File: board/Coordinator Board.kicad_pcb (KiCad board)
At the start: 4 copper layers, 45.5 x 39.6 mm, 30 parts, among them J1 Conn_01x04, J2 Conn_01x04, J3 Conn_01x04, P4 SERIAL, SW1 Switch_SPDT_x2, SW2 Switch_DPST, U0 10118194, U1 LM3671, U2 CD74HC4050, U3 ESP-12E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

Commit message: Finished and ordered v3.0 of the board!!
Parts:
- U2: moved to B.Cu
- moved J3 2.93 mm to (126.1, 132.4)
- moved C6 2.93 mm to (128.6, 136.2)
- moved D1 2.19 mm to (131.8, 121.8), turned to 180 degrees
- moved SW2 2.10 mm to (131.9, 118.7)
- moved U5 2.05 mm to (131.9, 110.0)
- moved U2 2.03 mm to (120.3, 135.9)
- moved R8 1.82 mm to (131.9, 124.2), turned to 180 degrees
- moved C4 1.45 mm to (110.8, 133.8)
- moved J2 1.35 mm to (114.7, 131.2)
- moved L1 1.05 mm to (107.0, 127.7)
- moved P4 0.68 mm to (130.4, 128.3)
- moved C5 0.25 mm to (101.8, 135.9)
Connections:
- U3 pad 13: Net-(RP1-Pad4) -> Net-(RP1-Pad3)
- U3 pad 14: Net-(RP1-Pad3) -> Net-(RP1-Pad4)
- U5 pad 1: Net-(R7-Pad2) -> Net-(RP1-Pad2)
- U5 pad 2: Net-(RP1-Pad2) -> Net-(RP1-Pad1)
- U5 pad 3: Net-(RP1-Pad1) -> Net-(R7-Pad2)
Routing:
- net Net-(D1-Pad2): track 41.6 -> 32.4 mm
- net Net-(R2-Pad1): track 39.6 -> 45.1 mm, vias 2 -> 3
- net Net-(U2-Pad3): track 13.9 -> 19.0 mm, vias 0 -> 3
- net Net-(J1-Pad2): track 23.8 -> 19.8 mm, vias 1 -> 0
- net Net-(U2-Pad11): track 17.0 -> 20.8 mm, vias 0 -> 3
- net GND: track 63.9 -> 60.4 mm, vias 7 -> 8
- net Net-(J3-Pad2): track 6.38 -> 3.21 mm
- net Net-(J1-Pad3): track 16.3 -> 13.6 mm
- net Net-(RP1-Pad2): track 44.7 -> 42.1 mm
- net Net-(R7-Pad2): track 45.5 -> 43.0 mm
- net Net-(J3-Pad3): track 12.0 -> 9.95 mm, vias 1 -> 0
- net Net-(RP1-Pad4): track 37.5 -> 36.0 mm
- net +5V: track 21.9 -> 23.2 mm, vias 4 -> 3
- net Net-(RP1-Pad1): track 48.6 -> 49.6 mm, vias 3 -> 2
- net Net-(J2-Pad2): track 14.7 -> 13.7 mm, vias 2 -> 1
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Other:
- board size 45.5 x 39.6 mm -> 42.5 x 38.5 mm
- board text added: "Raver Lights Hub v3.0 Copyright Bryan Hughes 2018"
- board text removed: "Raver Lights Coordinator v3.0 Copyright Bryan Hughes 2018"
- board text removed: "STS"

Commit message: Updated through first build
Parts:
- added C3: 0.1uF, Capacitors_SMD:C_0805_HandSoldering, F.Cu at (87.7, 125.6)
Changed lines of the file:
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@@
 (kicad_pcb (version 4) (host pcbnew 4.0.7)
   (general
-    (links 93)
-    (no_connects 0)
+    (links 95)
+    (no_connects 2)
     (area 93.869999 103.109999 136.515001 141.691001)
     (thickness 1.6)
@@
     (tracks 346)
     (zones 0)
-    (modules 30)
+    (modules 31)
     (nets 33)
   )
@@
   )
   (setup
-    (last_trace_width 0.3048)
+    (last_trace_width 0.1524)
     (user_trace_width 0.1524)
     (user_trace_width 0.3048)
@@
       (net 4 GND))
   )
+  (module Capacitors_SMD:C_0805_HandSoldering (layer F.Cu)
+    (at 87.697 125.639)
+    (descr "Capacitor SMD 0805, hand soldering")
+    (tags "capacitor 0805")
+    (attr smd)
+    (fp_text reference C3 (at 0 -1.75) (layer F.SilkS)
+      (effects (font (size 1 1) (thickness 0.15)))
+    )
+    (fp_text value 0.1uF (at 0 1.75) (layer F.Fab)
+      (effects (font (size 1 1) (thickness 0.15)))
+    )
+    (fp_text user %R (at 0 -1.75) (layer F.Fab)
+      (effects (font (size 1 1) (thickness 0.15)))
+    )
+    (fp_line (start -1 0.62) (end -1 -0.62) (layer F.Fab) (width 0.1))
+    (fp_line (start 1 0.62) (end -1 0.62) (layer F.Fab) (width 0.1))
+    (fp_line (start 1 -0.62) (end 1 0.62) (layer F.Fab) (width 0.1))
+    (fp_line (start -1 -0.62) (end 1 -0.62) (layer F.Fab) (width 0.1))
+    (fp_line (start 0.5 -0.85) (end -0.5 -0.85) (layer F.SilkS) (width 0.12))
+    (fp_line (start -0.5 0.85) (end 0.5 0.85) (layer F.SilkS) (width 0.12))
+    (fp_line (start -2.25 -0.88) (end 2.25 -0.88) (layer F.CrtYd) (width 0.05))
+    (fp_line (start -2.25 -0.88) (end -2.25 0.87) (layer F.CrtYd) (width 0.05))
+    (fp_line (start 2.25 0.87) (end 2.25 -0.88) (layer F.CrtYd) (width 0.05))
+    (fp_line (start 2.25 0.87) (end -2.25 0.87) (layer F.CrtYd) (width 0.05))
+    (pad 1 smd rect (at -1.25 0) (size 1.5 1.25) (layers F.Cu F.Paste F.Mask)
+      (net 5 +3V3))
+    (pad 2 smd rect (at 1.25 0) (size 1.5 1.25) (layers F.Cu F.Paste F.Mask)
+      (net 4 GND))
+    (model Capacitors_SMD.3dshapes/C_0805.wrl
+      (at (xyz 0 0 0))
+      (scale (xyz 1 1 1))
+      (rotate (xyz 0 0 0))
+    )
+  )
   (gr_text FUSE (at 97.73 117.13 90) (layer F.SilkS)

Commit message: Initial 3.1 board redesign
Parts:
- removed C3: 0.1uF, Capacitors_SMD:C_0805_HandSoldering
- removed C4, C5, C6: 10uF, Resistors_SMD:R_0805_HandSoldering
- removed D1: LED, LEDs:LED_1206_HandSoldering
- removed R1, R4, R7: 10k, Resistors_SMD:R_0805_HandSoldering
- removed R8: 0, Resistors_SMD:R_0805_HandSoldering
- removed U2: CD74HC4050, Housings_SOIC:SOIC-16W_5.3x10.2mm_Pitch1.27mm
- added J4: Conn_01x04, Pin_Headers:Pin_Header_Angled_1x04_Pitch2.54mm, F.Cu at (124.7, 131.2)
- added RV1: POT, nebrius-discrete:Model-35-Pot, F.Cu at (132.1, 119.4)
- U6: value SN74LVC1T45 -> SN74LVC1T45 - MOSI
- U7: value SN74LVC1T45 -> SN74LVC1T45 - SCLK
- moved SW2 6.24 mm to (132.4, 124.9)
- moved J3 1.42 mm to (127.4, 132.1)
- moved J1 1.40 mm to (102.9, 139.7)
- moved J2 1.40 mm to (113.4, 131.2)
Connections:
- J2 pad 2: Net-(J2-Pad2) -> Net-(J1-Pad2)
- J2 pad 3: Net-(J2-Pad3) -> Net-(J1-Pad3)
- J3 pad 2: Net-(J3-Pad2) -> Net-(J1-Pad2)
- J3 pad 3: Net-(J3-Pad3) -> Net-(J1-Pad3)
- RP1 pad 1: Net-(RP1-Pad1) -> GND
- RP1 pad 2: Net-(RP1-Pad2) -> GND
- RP1 pad 3: Net-(RP1-Pad3) -> GND
- RP1 pad 4: Net-(RP1-Pad4) -> +3V3
- RP1 pad 5: +3V3 -> Net-(RP1-Pad5)
- RP1 pad 6: +3V3 -> Net-(RP1-Pad6)
- RP1 pad 7: +3V3 -> Net-(RP1-Pad7)
- RP1 pad 8: +3V3 -> Net-(RP1-Pad8)
- U3 pad 10: Net-(R4-Pad1) -> Net-(RP1-Pad8)
- U3 pad 11: Net-(R1-Pad2) -> Net-(RP1-Pad5)
- U3 pad 13: Net-(RP1-Pad3) -> Net-(RP1-Pad7)
- U3 pad 14: Net-(RP1-Pad4) -> Net-(RP1-Pad6)
- U3 pad 19: Net-(R7-Pad2) -> (no net)
- U3 pad 2: (no net) -> Net-(RV1-Pad2)
- U3 pad 20: Net-(D1-Pad2) -> (no net)
- U3 pad 21: Net-(U3-Pad21) -> (no net)
- U3 pad 22: Net-(U3-Pad22) -> (no net)
- U3 pad 6: Net-(RP1-Pad2) -> Net-(U3-Pad6)
- U3 pad 7: Net-(RP1-Pad1) -> Net-(U3-Pad7)
- U4 pad 3: Net-(U3-Pad4) -> Net-(U3-Pad6)
- U4 pad 4: Net-(U3-Pad5) -> Net-(U3-Pad4)
- U5 pad 1: Net-(RP1-Pad2) -> (no net)
- U5 pad 2: Net-(RP1-Pad1) -> Net-(RP1-Pad8)
- U5 pad 3: Net-(R7-Pad2) -> Net-(RP1-Pad6)
- U5 pad 4: Net-(RP1-Pad4) -> Net-(RP1-Pad7)
- U5 pad 5: GND -> +3V3
- U5 pad 6: Net-(RP1-Pad3) -> (no net)
- U6 pad 3: Net-(U2-Pad11) -> Net-(J1-Pad3)
- U6 pad 4: Net-(U3-Pad21) -> Net-(U3-Pad7)
- U7 pad 3: Net-(U2-Pad3) -> Net-(J1-Pad2)
- U7 pad 4: Net-(U3-Pad22) -> Net-(U3-Pad5)
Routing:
- net GND: track 60.4 -> 0.00 mm, vias 8 -> 0
- net Net-(RP1-Pad1): track 49.6 -> 0.00 mm, vias 2 -> 0
- net Net-(U3-Pad22): track 45.5 -> 0.00 mm, vias 1 -> 0
- net Net-(R2-Pad1): track 45.1 -> 0.00 mm, vias 3 -> 0
- net Net-(R7-Pad2): track 43.0 -> 0.00 mm, vias 2 -> 0
- net Net-(RP1-Pad3): track 42.4 -> 0.00 mm, vias 2 -> 0
- net Net-(RP1-Pad2): track 42.1 -> 0.00 mm, vias 2 -> 0
- net Net-(U3-Pad21): track 41.4 -> 0.00 mm, vias 1 -> 0
- net Net-(P4-Pad2): track 36.1 -> 0.00 mm, vias 1 -> 0
- net Net-(RP1-Pad4): track 36.0 -> 0.00 mm, vias 2 -> 0
- net Net-(P4-Pad1): track 34.2 -> 0.00 mm, vias 1 -> 0
- net Net-(D1-Pad2): track 32.4 -> 0.00 mm, vias 1 -> 0
- net +3V3: track 29.7 -> 0.00 mm, vias 5 -> 0
- net +5V: track 23.2 -> 0.00 mm, vias 3 -> 0
- net Net-(U2-Pad11): track 20.8 -> 0.00 mm, vias 3 -> 0
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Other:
- board text added: "Raver Lights Hub v3.1 Copyright Bryan Hughes 2018"
- board text removed: "Raver Lights Hub v3.0 Copyright Bryan Hughes 2018"

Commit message: Finished v3.1 of the board
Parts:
- moved R2 1.25 mm to (108.9, 111.4)
- moved RV1 0.18 mm to (132.3, 119.5), turned to 180 degrees
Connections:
- U4 pad 3: Net-(U3-Pad6) -> Net-(U3-Pad4)
- U4 pad 4: Net-(U3-Pad4) -> Net-(U3-Pad6)
- U5 pad 1: (no net) -> Net-(RP1-Pad6)
- U5 pad 3: Net-(RP1-Pad6) -> (no net)
- U5 pad 4: Net-(RP1-Pad7) -> (no net)
- U5 pad 6: (no net) -> Net-(RP1-Pad7)
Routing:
- net Net-(J1-Pad2): track 0.00 -> 49.6 mm
- net Net-(RP1-Pad8): track 0.00 -> 41.5 mm, vias 0 -> 2
- net +3V3: track 0.00 -> 41.2 mm, vias 0 -> 8
- net Net-(J1-Pad3): track 0.00 -> 40.9 mm
- net Net-(RP1-Pad7): track 0.00 -> 40.8 mm, vias 0 -> 1
- net Net-(R2-Pad1): track 0.00 -> 40.8 mm, vias 0 -> 1
- net Net-(RP1-Pad6): track 0.00 -> 39.1 mm, vias 0 -> 1
- net GND: track 0.00 -> 37.0 mm, vias 0 -> 8
- net Net-(P4-Pad2): track 0.00 -> 31.1 mm
- net Net-(P4-Pad1): track 0.00 -> 30.6 mm
- net Net-(U3-Pad7): track 0.00 -> 20.8 mm, vias 0 -> 1
- net Net-(U3-Pad5): track 0.00 -> 20.5 mm, vias 0 -> 1
- net Net-(RV1-Pad2): track 0.00 -> 19.9 mm, vias 0 -> 1
- net +5V: track 0.00 -> 14.1 mm, vias 0 -> 3
- net Net-(RP1-Pad5): track 0.00 -> 9.08 mm, vias 0 -> 1
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
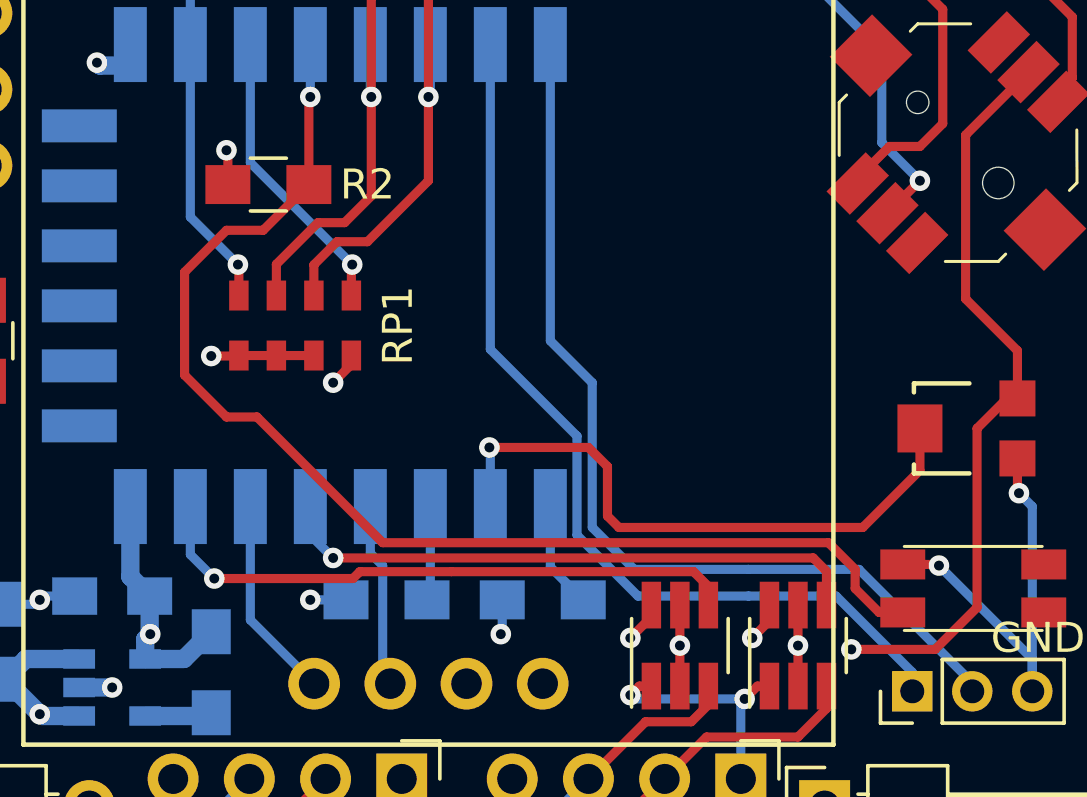
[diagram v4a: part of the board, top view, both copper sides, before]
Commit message: Updated r array footprint
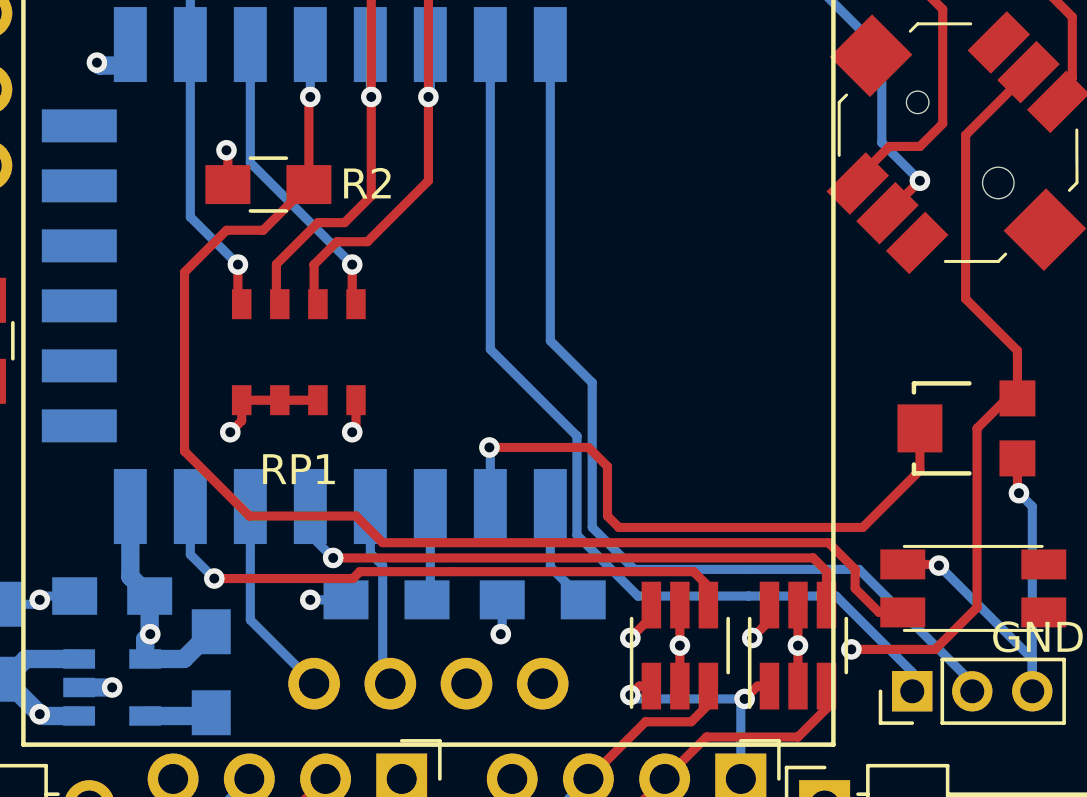
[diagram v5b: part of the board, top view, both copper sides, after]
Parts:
- RP1: footprint nebrius-discrete:R_Array_Concave_4x0805 -> nebrius-discrete:R_Array_Concave_4x2012.kicad_mod
- moved RP1 0.89 mm to (109.9, 117.0)
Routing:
- net Net-(R2-Pad1): track 40.8 -> 42.3 mm
